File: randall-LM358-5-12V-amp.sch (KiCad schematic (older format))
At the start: 27 parts, among them J1 Barrel_Jack, M1 Fan_3pin, M2 Fan_3pin, Q1 TIP120, Q2 TIP120, U1 LM2674M-3.3, U2 LM358, U3 Z-Uno

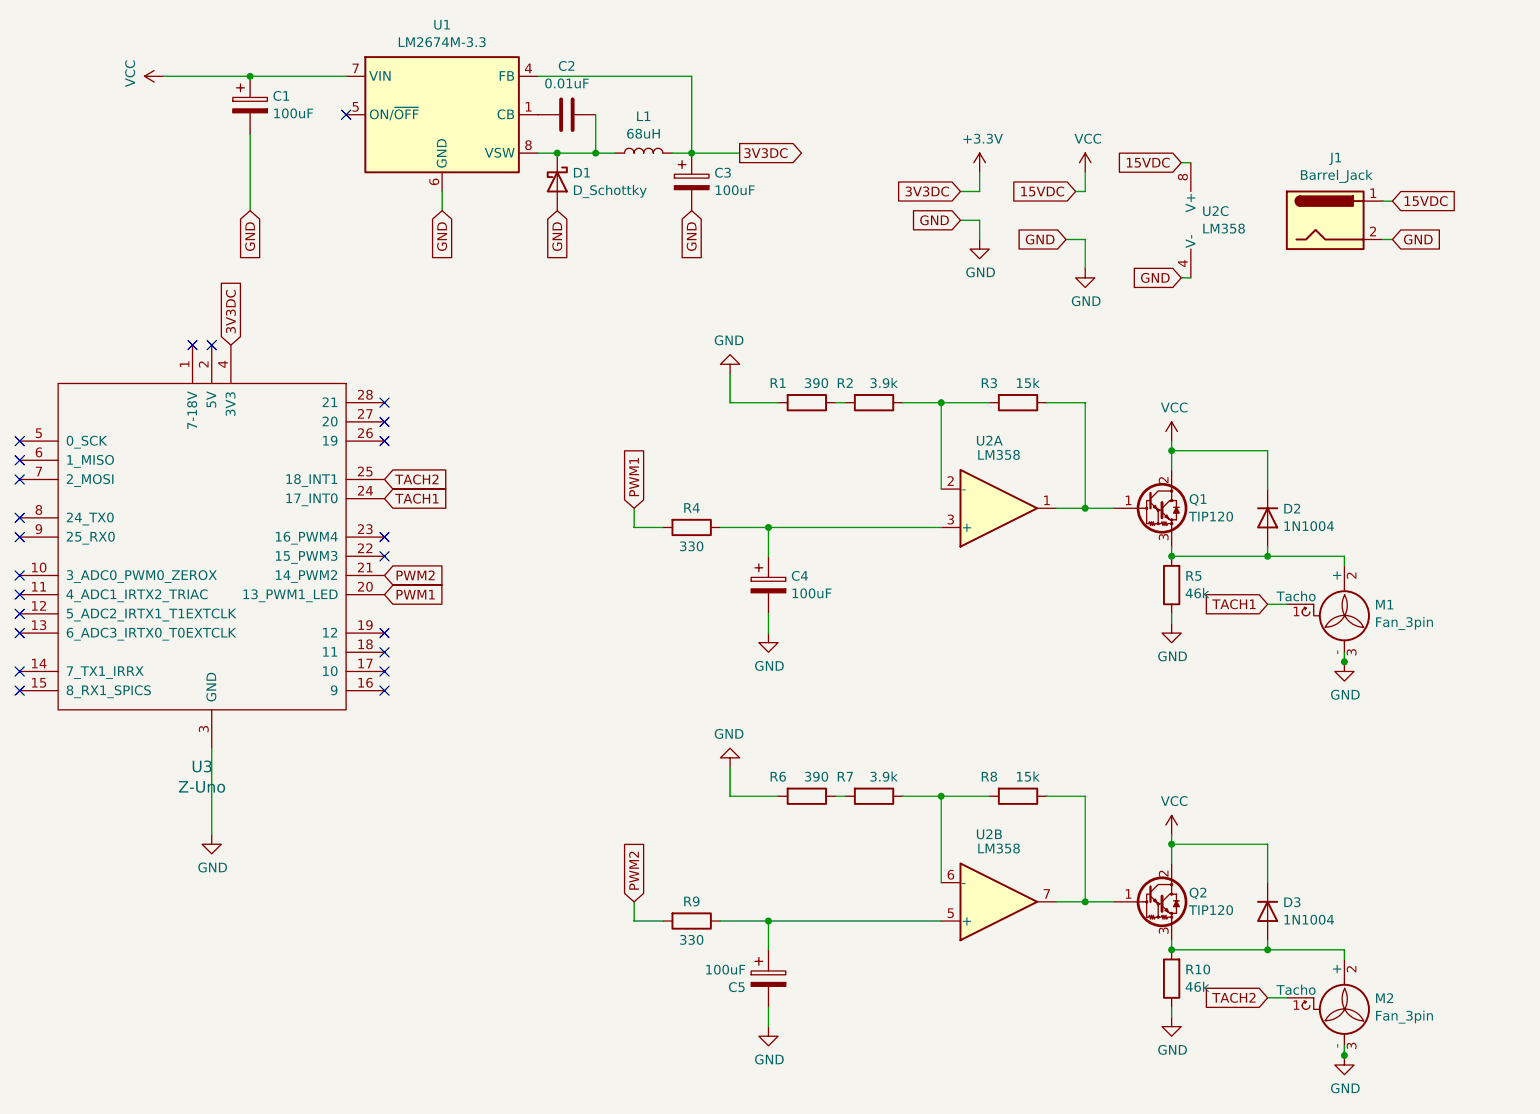
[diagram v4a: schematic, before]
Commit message: Updated with P/Ns where necessary
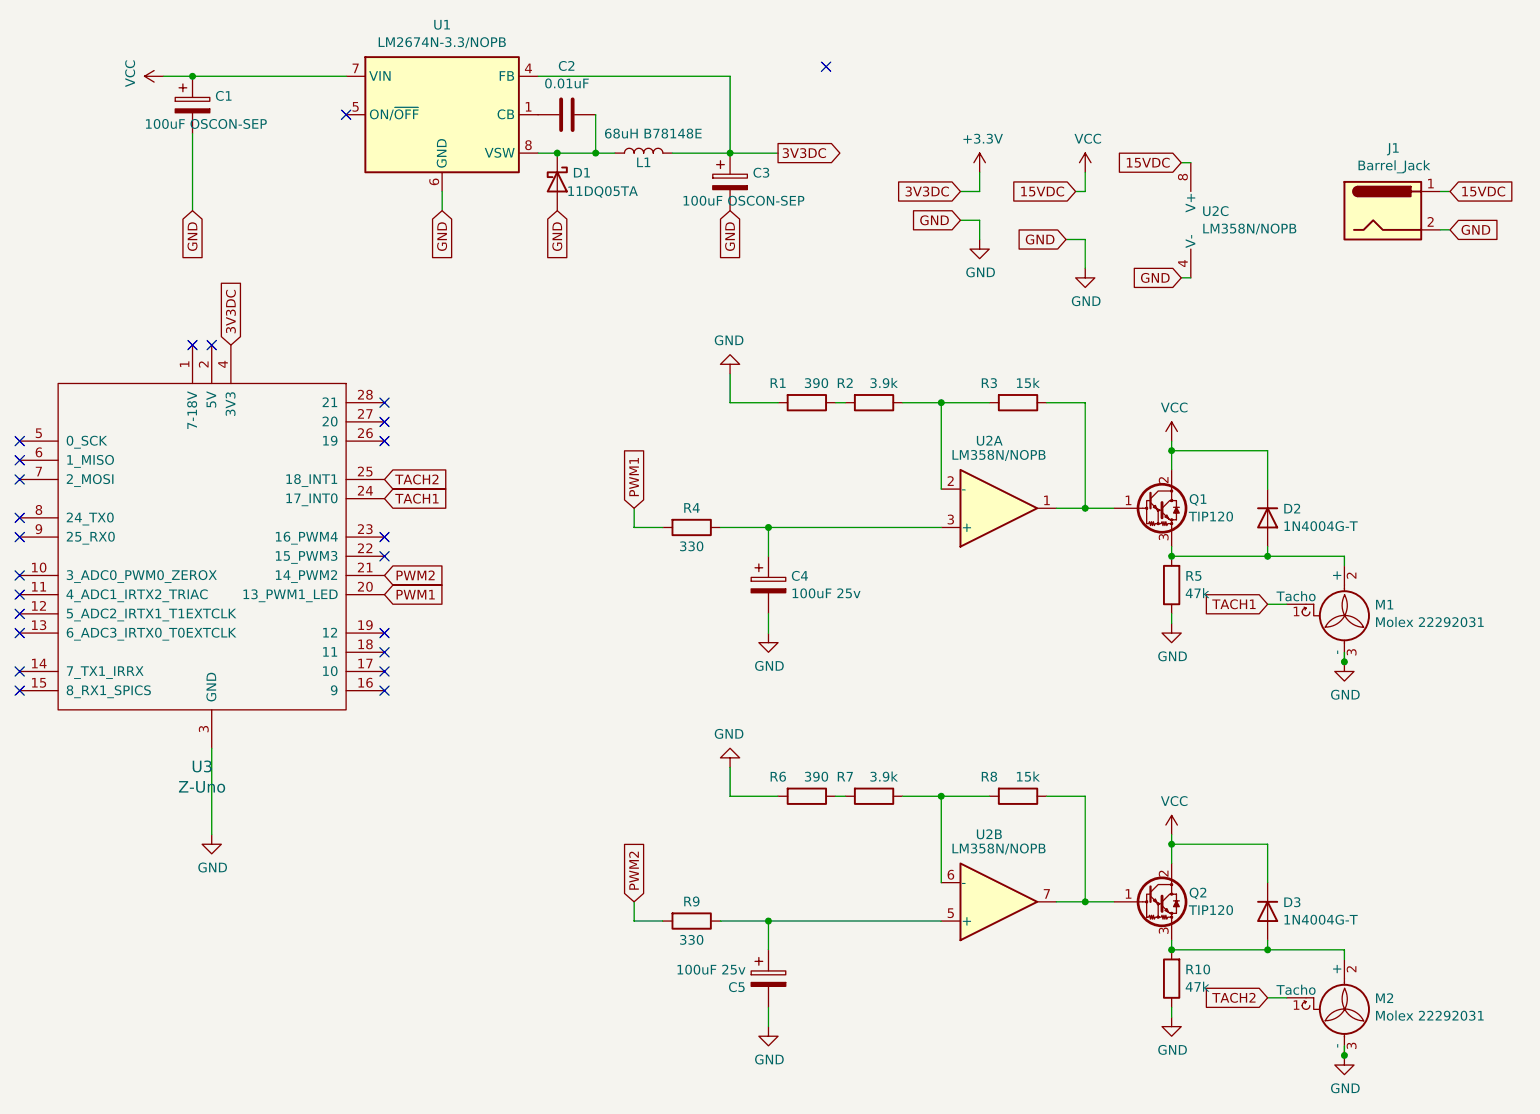
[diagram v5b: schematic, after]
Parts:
- C1, C3: value 100uF -> 100uF OSCON-SEP
- C4, C5: value 100uF -> 100uF 25v
- D1: value D_Schottky -> 11DQ05TA
- D2, D3: value 1N1004 -> 1N4004G-T
- J1: footprint Connector_BarrelJack:BarrelJack_CUI_PJ-063AH_Horizontal_CircularHoles -> TerminalBlock:TerminalBlock_Altech_AK300-2_P5.00mm
- L1: value 68uH -> 68uH B78148E
- M1, M2: value Fan_3pin -> Molex 22292031
- R10, R5: value 46k -> 47k
- U1: value LM2674M-3.3 -> LM2674N-3.3/NOPB
- U2: value LM358 -> LM358N/NOPB
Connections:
- no-connect marks 23 -> 24
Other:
- moved on the sheet: C1, C3, J1
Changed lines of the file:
@@
 P 6850 1700
 F 0 "U2" H 6808 1746 50  0000 L CNN
-F 1 "LM358" H 6808 1655 50  0000 L CNN
+F 1 "LM358N/NOPB" H 6808 1655 50  0000 L CNN
 F 2 "Package_DIP:DIP-8_W7.62mm_Socket" H 6850 1700 50  0001 C CNN
 F 3 "http://www.ti.com/lit/ds/symlink/lm2904-n.pdf" H 6850 1700 50  0001 C CNN
@@
 P 6650 3600
 F 0 "R5" H 6580 3554 50  0000 R CNN
-F 1 "46k" H 6580 3645 50  0000 R CNN
+F 1 "47k" H 6580 3645 50  0000 R CNN
 F 2 "Resistor_THT:R_Axial_DIN0207_L6.3mm_D2.5mm_P7.62mm_Horizontal" V 6580 3600 50  0001 C CNN
 F 3 "~" H 6650 3600 50  0001 C CNN
@@
 P 7150 3250
 F 0 "D2" V 7104 3330 50  0000 L CNN
-F 1 "1N1004" V 7195 3330 50  0000 L CNN
+F 1 "1N4004G-T" V 7195 3330 50  0000 L CNN
 F 2 "Diode_THT:D_A-405_P7.62mm_Horizontal" H 7150 3250 50  0001 C CNN
 F 3 "~" H 7150 3250 50  0001 C CNN
@@
 	5650 1700 5650 1800
 Wire Wire Line
-	7800 1800 7750 1800
-Wire Wire Line
-	7750 1600 7800 1600
+	8100 1750 8050 1750
+Wire Wire Line
+	8050 1550 8100 1550
 Text GLabel 2550 3650 2    50   Input ~ 0
 PWM1
@@
 P 7550 3700
 F 0 "M1" H 7708 3696 50  0000 L CNN
-F 1 "Fan_3pin" H 7708 3605 50  0000 L CNN
+F 1 "Molex 22292031" H 7708 3605 50  0000 L CNN
 F 2 "Connector_Molex:Molex_KK-254_AE-6410-03A_1x03_P2.54mm_Vertical" H 7550 3610 50  0001 C CNN
 F 3 "http://www.hardwarecanucks.com/forum/attachments/new-builds/16287d1330775095-help-chassis-power-fan-connectors-motherboard-asus_p8z68.jpg" H 7550 3610 50  0001 C CNN
@@
 P 4550 3600
 F 0 "C4" H 4668 3646 50  0000 L CNN
-F 1 "100uF" H 4668 3555 50  0000 L CNN
+F 1 "100uF 25v" H 4668 3555 50  0000 L CNN
 F 2 "Capacitor_THT:CP_Radial_D5.0mm_P2.00mm" H 4588 3450 50  0001 C CNN
 F 3 "~" H 4550 3600 50  0001 C CNN
@@
 P 5750 3200
 F 0 "U2" H 5700 2850 50  0000 C CNN
-F 1 "LM358" H 5750 2924 50  0000 C CNN
+F 1 "LM358N/NOPB" H 5750 2924 50  0000 C CNN
 F 2 "Package_DIP:DIP-8_W7.62mm_Socket" H 5750 3200 50  0001 C CNN
 F 3 "http://www.ti.com/lit/ds/symlink/lm2904-n.pdf" H 5750 3200 50  0001 C CNN
@@
 P 6650 5650
 F 0 "R10" H 6580 5604 50  0000 R CNN
-F 1 "46k" H 6580 5695 50  0000 R CNN
+F 1 "47k" H 6580 5695 50  0000 R CNN
 F 2 "Resistor_THT:R_Axial_DIN0207_L6.3mm_D2.5mm_P7.62mm_Horizontal" V 6580 5650 50  0001 C CNN
 F 3 "~" H 6650 5650 50  0001 C CNN
@@
 P 7150 5300
 F 0 "D3" V 7104 5380 50  0000 L CNN
-F 1 "1N1004" V 7195 5380 50  0000 L CNN
+F 1 "1N4004G-T" V 7195 5380 50  0000 L CNN
 F 2 "Diode_THT:D_A-405_P7.62mm_Horizontal" H 7150 5300 50  0001 C CNN
 F 3 "~" H 7150 5300 50  0001 C CNN
@@
 P 7550 5750
 F 0 "M2" H 7708 5746 50  0000 L CNN
-F 1 "Fan_3pin" H 7708 5655 50  0000 L CNN
+F 1 "Molex 22292031" H 7708 5655 50  0000 L CNN
 F 2 "Connector_Molex:Molex_KK-254_AE-6410-03A_1x03_P2.54mm_Vertical" H 7550 5660 50  0001 C CNN
 F 3 "http://www.hardwarecanucks.com/forum/attachments/new-builds/16287d1330775095-help-chassis-power-fan-connectors-motherboard-asus_p8z68.jpg" H 7550 5660 50  0001 C CNN
@@
 P 4550 5650
 F 0 "C5" H 4432 5604 50  0000 R CNN
-F 1 "100uF" H 4432 5695 50  0000 R CNN
+F 1 "100uF 25v" H 4432 5695 50  0000 R CNN
 F 2 "Capacitor_THT:CP_Radial_D5.0mm_P2.00mm" H 4588 5500 50  0001 C CNN
 F 3 "~" H 4550 5650 50  0001 C CNN
@@
 P 5750 5250
 F 0 "U2" H 5700 4900 50  0000 C CNN
-F 1 "LM358" H 5750 4974 50  0000 C CNN
+F 1 "LM358N/NOPB" H 5750 4974 50  0000 C CNN
 F 2 "Package_DIP:DIP-8_W7.62mm_Socket" H 5750 5250 50  0001 C CNN
 F 3 "http://www.ti.com/lit/ds/symlink/lm2904-n.pdf" H 5750 5250 50  0001 C CNN
@@
 P 2850 1150
 F 0 "U1" H 2850 1617 50  0000 C CNN
-F 1 "LM2674M-3.3" H 2850 1526 50  0000 C CNN
+F 1 "LM2674N-3.3/NOPB" H 2850 1526 50  0000 C CNN
 F 2 "Package_DIP:DIP-8_W7.62mm_Socket" H 2900 800 50  0001 L CIN
 F 3 "http://www.ti.com/lit/ds/symlink/lm2674.pdf" H 2850 1150 50  0001 C CNN
@@
 L Device:CP C1
 U 1 1 6086CCED
-P 1850 1100
-F 0 "C1" H 1968 1146 50  0000 L CNN
-F 1 "100uF" H 1968 1055 50  0000 L CNN
-F 2 "Capacitor_THT:CP_Radial_D5.0mm_P2.00mm" H 1888 950 50  0001 C CNN
-F 3 "~" H 1850 1100 50  0001 C CNN
-	1    1850 1100
-	1    0    0    -1
-$EndComp
-Text GLabel 1850 1650 3    50   Input ~ 0
+P 1550 1100
+F 0 "C1" H 1668 1146 50  0000 L CNN
+F 1 "100uF OSCON-SEP" H 1300 1000 50  0000 L CNN
+F 2 "Capacitor_THT:CP_Radial_D5.0mm_P2.00mm" H 1588 950 50  0001 C CNN
+F 3 "https://industrial.panasonic.com/ww/products/capacitors/polymer-capacitors/os-con/models/20SEP100M" H 1550 1100 50  0001 C CNN
+	1    1550 1100
+	1    0    0    -1
+$EndComp
+Text GLabel 1550 1650 3    50   Input ~ 0
 GND
 Wire Wire Line
-	1400 950  1850 950
-Connection ~ 1850 950
-Wire Wire Line
-	1850 950  2350 950
+	1400 950  1550 950
+Connection ~ 1550 950
+Wire Wire Line
+	1550 950  2350 950
 $Comp
 L Device:C C2
@@
 Wire Wire Line
 	3350 1350 3450 1350
-Text GLabel 4150 1650 3    50   Input ~ 0
+Text GLabel 4350 1650 3    50   Input ~ 0
 GND
 Wire Wire Line
-	1850 1250 1850 1650
+	1550 1250 1550 1650
 Wire Wire Line
 	2850 1550 2850 1650
-Text GLabel 4400 1350 2    50   Output ~ 0
+Text GLabel 4600 1350 2    50   Output ~ 0
 3V3DC
 $Comp
@@
 	0    -1   -1   0
 $EndComp
-Text GLabel 7800 1600 2    50   Input ~ 0
+Text GLabel 8100 1550 2    50   Input ~ 0
 15VDC
-Text GLabel 7800 1800 2    50   Input ~ 0
+Text GLabel 8100 1750 2    50   Input ~ 0
 GND
 $Comp
@@
 P 3450 1500
 F 0 "D1" V 3404 1580 50  0000 L CNN
-F 1 "D_Schottky" V 3495 1580 50  0000 L CNN
+F 1 "11DQ05TA" V 3500 1550 50  0000 L CNN
 F 2 "Diode_THT:D_A-405_P7.62mm_Horizontal" H 3450 1500 50  0001 C CNN
 F 3 "~" H 3450 1500 50  0001 C CNN
@@
 L Device:CP C3
 U 1 1 6087ABE3
-P 4150 1500
-F 0 "C3" H 4268 1546 50  0000 L CNN
-F 1 "100uF" H 4268 1455 50  0000 L CNN
-F 2 "Capacitor_THT:CP_Radial_D5.0mm_P2.00mm" H 4188 1350 50  0001 C CNN
-F 3 "~" H 4150 1500 50  0001 C CNN
-	1    4150 1500
-	1    0    0    -1
-$EndComp
-Wire Wire Line
-	4150 950  4150 1350
-Wire Wire Line
-	3350 950  4150 950
-Connection ~ 4150 1350
-Wire Wire Line
-	4150 1350 4400 1350
+P 4350 1500
+F 0 "C3" H 4468 1546 50  0000 L CNN
+F 1 "100uF OSCON-SEP" H 4100 1400 50  0000 L CNN
+F 2 "Capacitor_THT:CP_Radial_D5.0mm_P2.00mm" H 4388 1350 50  0001 C CNN
+F 3 "https://industrial.panasonic.com/ww/products/capacitors/polymer-capacitors/os-con/models/20SEP100M" H 4350 1500 50  0001 C CNN
+	1    4350 1500
+	1    0    0    -1
+$EndComp
+Wire Wire Line
+	4350 950  4350 1350
+Wire Wire Line
+	3350 950  4350 950
+Connection ~ 4350 1350
+Wire Wire Line
+	4350 1350 4600 1350
 $Comp
 L Device:L L1
 U 1 1 60877FA2
 P 3900 1350
-F 0 "L1" V 4090 1350 50  0000 C CNN
-F 1 "68uH" V 3999 1350 50  0000 C CNN
+F 0 "L1" V 3850 1350 50  0000 C CNN
+F 1 "68uH B78148E" V 4000 1300 50  0000 C CNN
 F 2 "Inductor_THT:L_Axial_L14.0mm_D4.5mm_P5.08mm_Vertical_Fastron_LACC" H 3900 1350 50  0001 C CNN
-F 3 "~" H 3900 1350 50  0001 C CNN
+F 3 "https://www.tdk-electronics.tdk.com/inf/30/ds/b78108_148e.pdf" H 3900 1350 50  0001 C CNN
 	1    3900 1350
 	0    -1   -1   0
@@
 	3750 1350 3650 1350
 Wire Wire Line
-	4050 1350 4150 1350
+	4050 1350 4350 1350
 $Comp
 L Connector:Barrel_Jack J1
 U 1 1 6050E38F
-P 7450 1700
-F 0 "J1" H 7507 2025 50  0000 C CNN
-F 1 "Barrel_Jack" H 7507 1934 50  0000 C CNN
-F 2 "Connector_BarrelJack:BarrelJack_CUI_PJ-063AH_Horizontal_CircularHoles" H 7500 1660 50  0001 C CNN
-F 3 "~" H 7500 1660 50  0001 C CNN
-	1    7450 1700
+P 7750 1650
+F 0 "J1" H 7807 1975 50  0000 C CNN
+F 1 "Barrel_Jack" H 7807 1884 50  0000 C CNN
+F 2 "TerminalBlock:TerminalBlock_Altech_AK300-2_P5.00mm" H 7800 1610 50  0001 C CNN
+F 3 "~" H 7800 1610 50  0001 C CNN
+	1    7750 1650
 	1    0    0    -1
 $EndComp
@@
 	0    1    1    0
 $EndComp
+NoConn ~ 4850 900
 $EndSCHEMATC
